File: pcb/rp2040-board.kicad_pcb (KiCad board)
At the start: 4 copper layers, 75 x 48 mm, 51 parts, among them J1 DMX, J2 GPIO, J3 ELRS, J4 OLED, J5 SWD, J6 USB_C_Receptacle_USB2.0_16P, SW1 USB Boot, SW2 RotaryEncoder_Switch, SW3 Reset, U1 W25Q128JVS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

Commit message: board rc3
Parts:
- added C20: 4.7n, Capacitor_SMD:C_0402_1005Metric, F.Cu at (158.4, 86.2)
- added C21: 4.7n, Capacitor_SMD:C_0402_1005Metric, F.Cu at (166.8, 86.2)
- added C22: 22u, Capacitor_SMD:C_0805_2012Metric, F.Cu at (169.0, 82.6)
- added C23: 100n, Capacitor_SMD:C_0402_1005Metric, F.Cu at (161.2, 79.0)
- added C24: 1u, Capacitor_SMD:C_0402_1005Metric, F.Cu at (164.0, 79.0)
- added J7: AUDIO, Connector_PinHeader_2.54mm:PinHeader_1x02_P2.54mm_Vertical, F.Cu at (172.2, 81.3)
- added R14: 1k5, Resistor_SMD:R_0402_1005Metric, F.Cu at (164.0, 86.2)
- added R15: 1k5, Resistor_SMD:R_0402_1005Metric, F.Cu at (161.2, 86.2)
- added R16: 0, Resistor_SMD:R_0603_1608Metric, F.Cu at (154.2, 79.0)
- added U5: OP07CDR, Package_SO:SOIC-8_3.9x4.9mm_P1.27mm, F.Cu at (162.6, 82.6)
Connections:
- U3 pad 41: unconnected-(U3-GPIO29_ADC3-Pad41) -> PWM_AUDIO
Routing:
- net PWM_AUDIO: track 0.00 -> 24.3 mm, vias 0 -> 2
- net Net-(U5-V+): track 0.00 -> 13.4 mm
- net Net-(U5--): track 0.00 -> 13.2 mm
- net Net-(U5-+): track 0.00 -> 9.69 mm
- net ELRS_RX: track 30.7 -> 37.3 mm
- net ELRS_TX: track 33.0 -> 39.4 mm
- net GND: track 80.5 -> 86.8 mm, vias 69 -> 73
- net Net-(C21-Pad1): track 0.00 -> 5.12 mm
- net Net-(J7-Pin_1): track 0.00 -> 3.33 mm
- net +5V: track 95.2 -> 97.3 mm, vias 2 -> 3
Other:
- board text added: "github.com/barycz/rp2040-board Tomas Barak, 2024"

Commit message: board rc4, BOM cleanup
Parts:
- SW1: value USB Boot -> TS-1187A-B-A-B
- SW3: value Reset -> TS-1187A-B-A-B
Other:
- board text added: "GND 3V3 SCK SDA"
- board text added: "GND 5V ERX ETX"
- board text added: "Reset"
- board text added: "USB Boot"

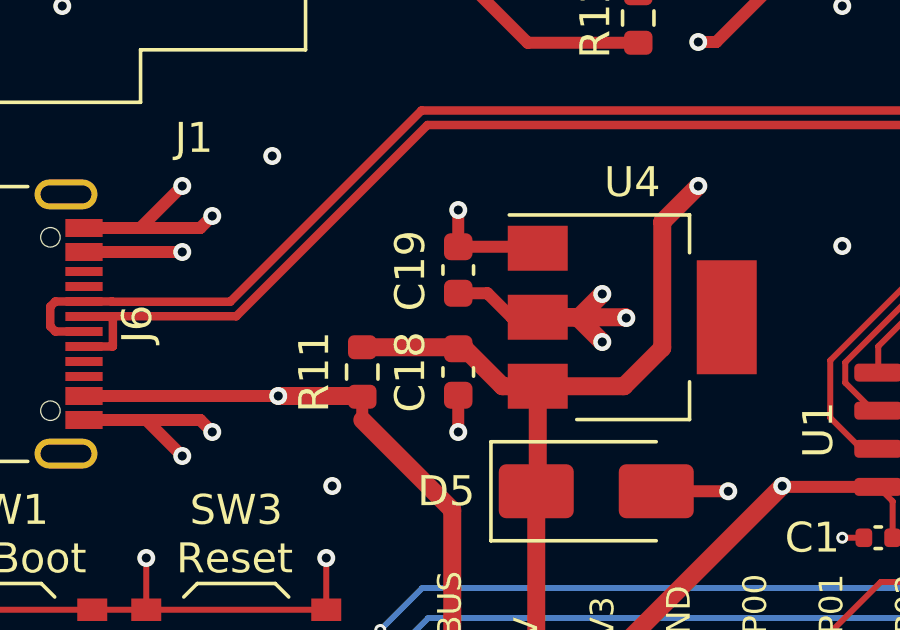
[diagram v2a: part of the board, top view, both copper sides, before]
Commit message: enlarge power supply caps
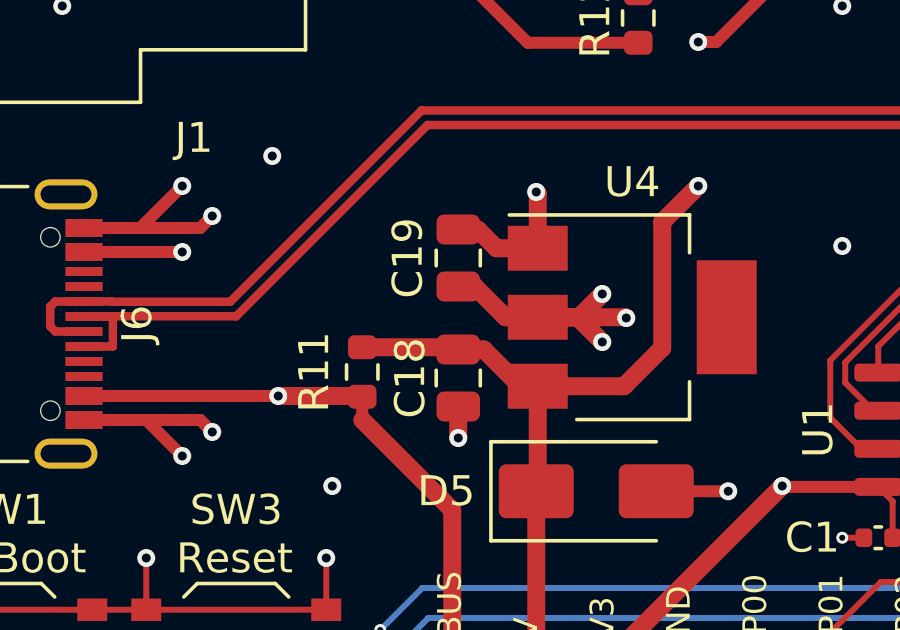
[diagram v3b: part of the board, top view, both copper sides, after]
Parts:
- C18, C19: value 10u -> 22u; footprint Capacitor_SMD:C_0603_1608Metric -> Capacitor_SMD:C_0805_2012Metric
- moved C19 0.40 mm to (119.2, 103.4)
- moved C18 0.20 mm to (119.2, 107.4)
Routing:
- net +3V3: track 169.6 -> 170.6 mm
- net GND: track 86.8 -> 87.6 mm

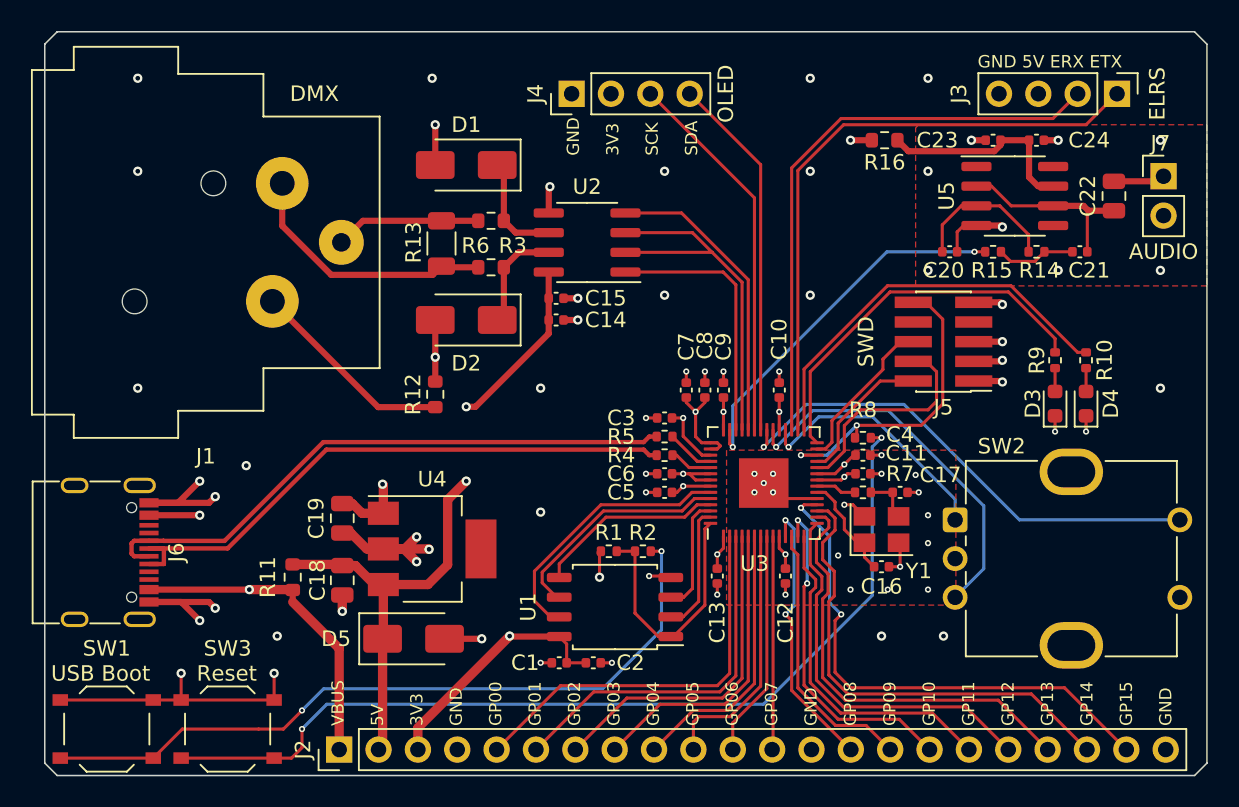
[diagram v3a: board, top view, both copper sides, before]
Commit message: fixed pin assignment issues
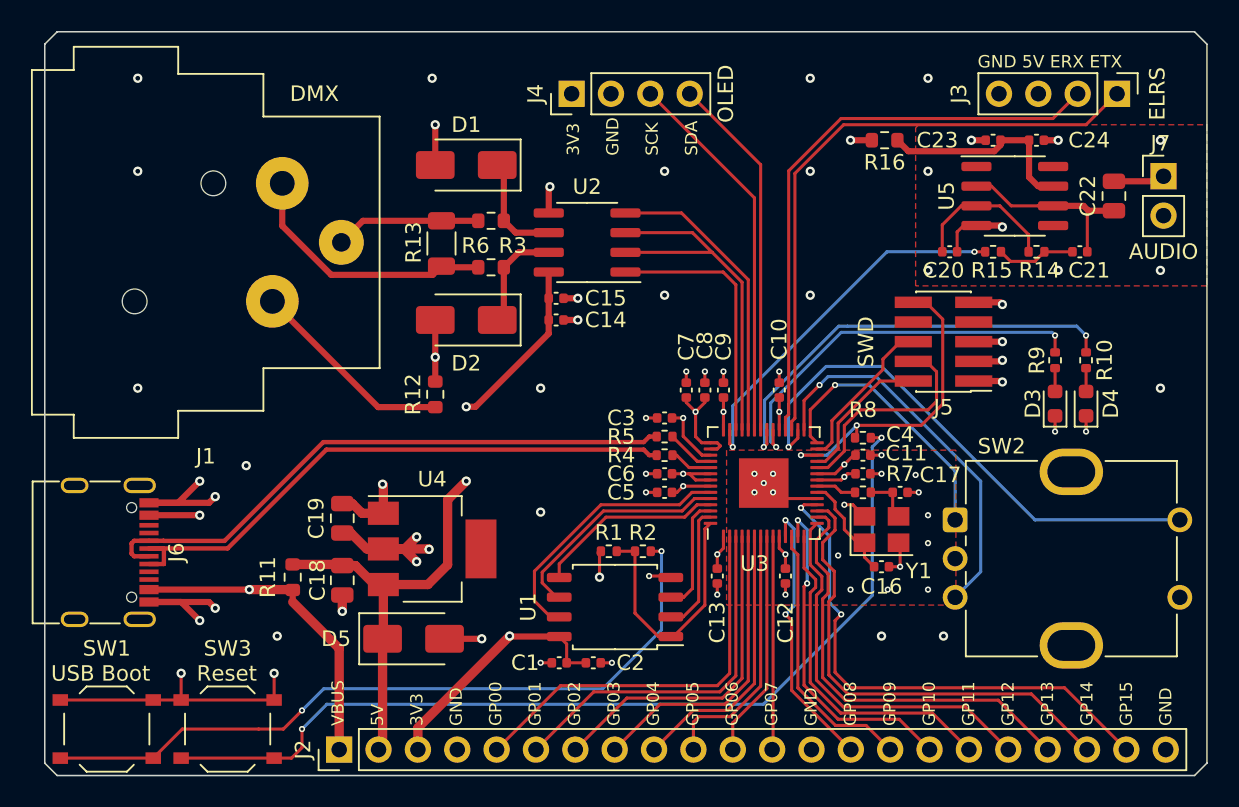
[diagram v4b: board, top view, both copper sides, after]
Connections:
- J4 pad 1: GND -> +3V3
- J4 pad 2: +3V3 -> GND
- U3 pad 28: LED_D1 -> RE_A
- U3 pad 29: LED_D2 -> RE_B
- U3 pad 30: ELRS_TX -> RE_SW
- U3 pad 31: ELRS_RX -> ELRS_TX
- U3 pad 32: RE_A -> ELRS_RX
- U3 pad 34: RE_B -> LED_D1
- U3 pad 35: RE_SW -> LED_D2
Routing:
- net LED_D2: track 26.1 -> 28.4 mm, vias 0 -> 2
- net RE_SW: track 32.3 -> 34.5 mm
- net RE_A: track 16.3 -> 17.8 mm
- net +3V3: track 170.6 -> 169.5 mm
- net LED_D1: track 24.8 -> 25.6 mm, vias 0 -> 2
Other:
- board text added: "3V3 GND SCK SDA"
- board text removed: "GND 3V3 SCK SDA"

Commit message: pin assignment issues fixed
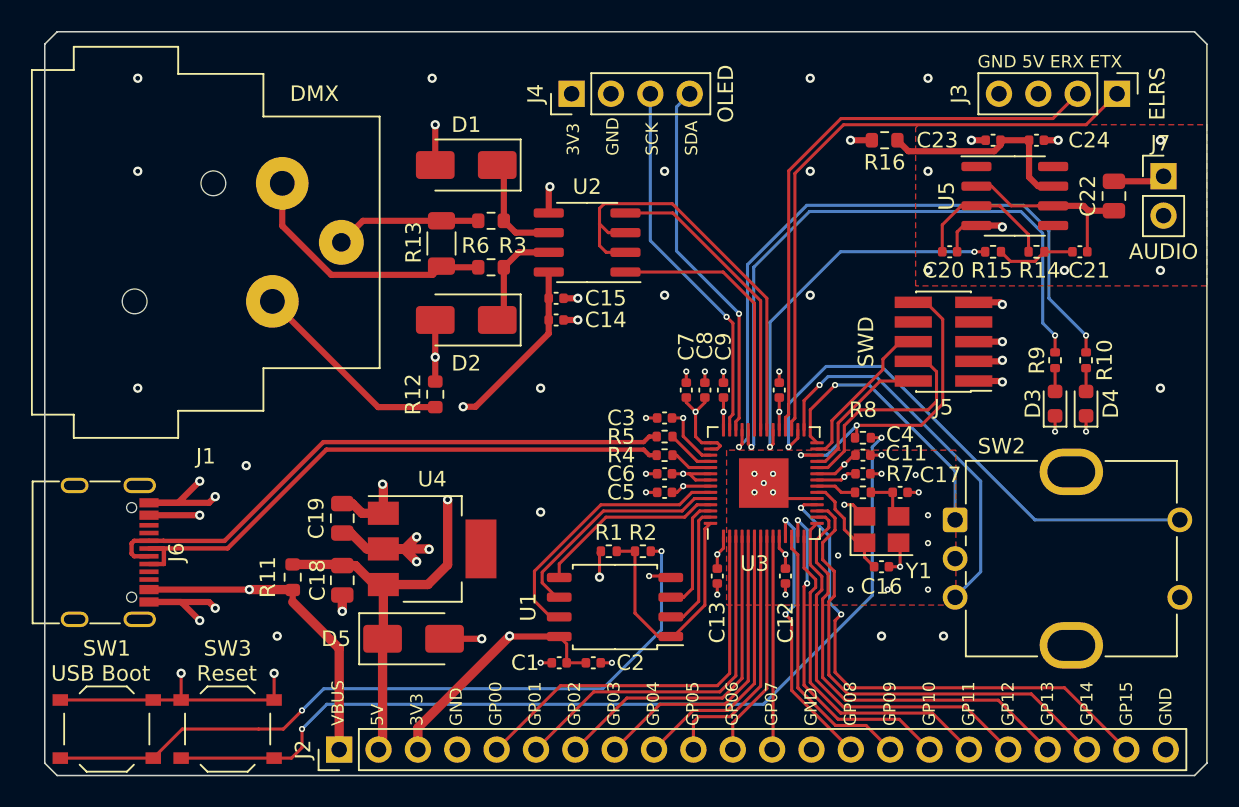
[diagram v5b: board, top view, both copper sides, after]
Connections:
- U2 pad 2: RS485_RE_NDE -> RS485_NRE_DE
- U2 pad 3: RS485_RE_NDE -> RS485_NRE_DE
- U3 pad 34: LED_D1 -> PWM_AUDIO
- U3 pad 35: LED_D2 -> RS485_NRE_DE
- U3 pad 36: OLED_SDA -> RS485_TXD
- U3 pad 37: OLED_SCK -> RS485_RXD
- U3 pad 38: RS485_TXD -> LED_D1
- U3 pad 39: RS485_RE_NDE -> LED_D2
- U3 pad 40: RS485_RXD -> OLED_SDA
- U3 pad 41: PWM_AUDIO -> OLED_SCK
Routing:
- net RS485_NRE_DE: track 0.00 -> 28.1 mm
- net RS485_RE_NDE: track 24.0 -> 0.00 mm
- net LED_D1: track 25.6 -> 41.6 mm
- net LED_D2: track 28.4 -> 43.8 mm
- net PWM_AUDIO: track 24.3 -> 25.0 mm
- net OLED_SCK: track 24.5 -> 24.0 mm, vias 0 -> 1
- net OLED_SDA: track 23.6 -> 23.8 mm, vias 0 -> 1

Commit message: board rc5
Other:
- board text added: "JLCJLCJLCJLC"

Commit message: fabrication tweaks
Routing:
- net +3V3: track 169.5 -> 178.1 mm
- net +1V1: track 26.9 -> 30.3 mm
- net GND: vias 73 -> 75

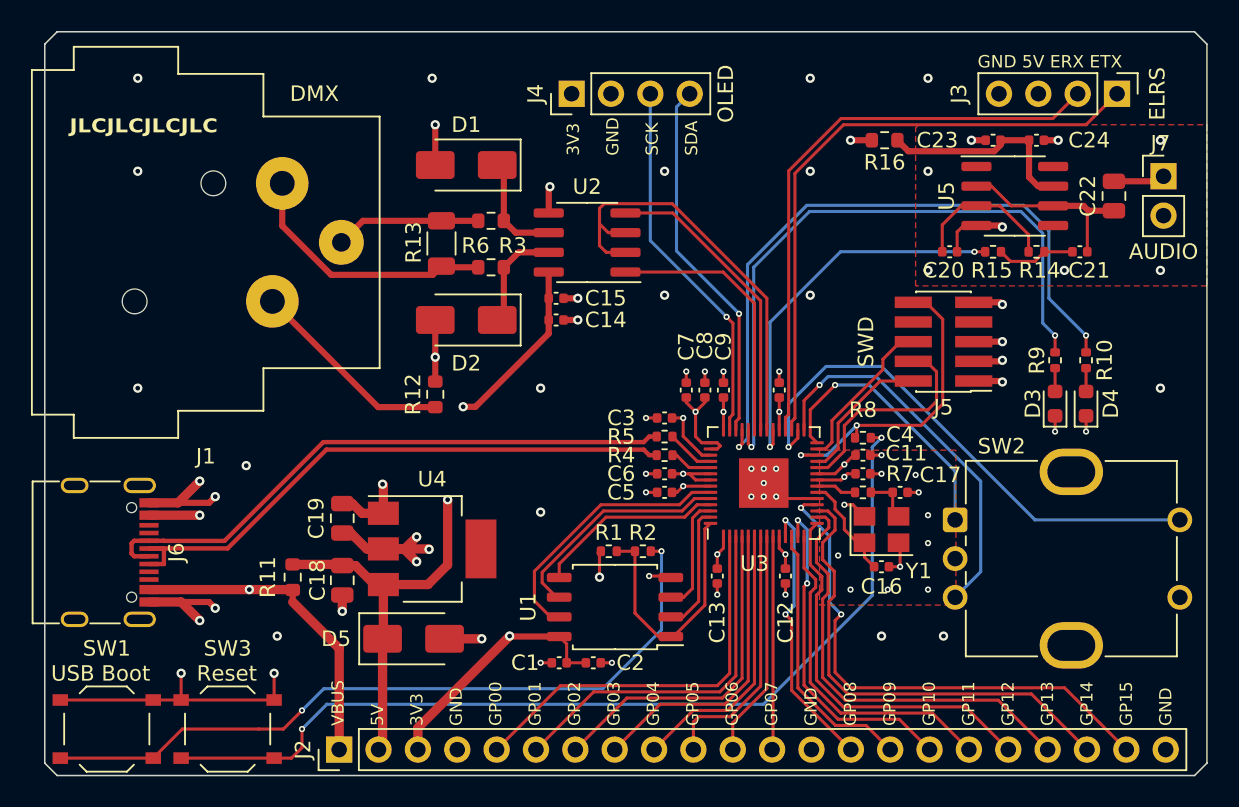
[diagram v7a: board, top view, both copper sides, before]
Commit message: fixed via size
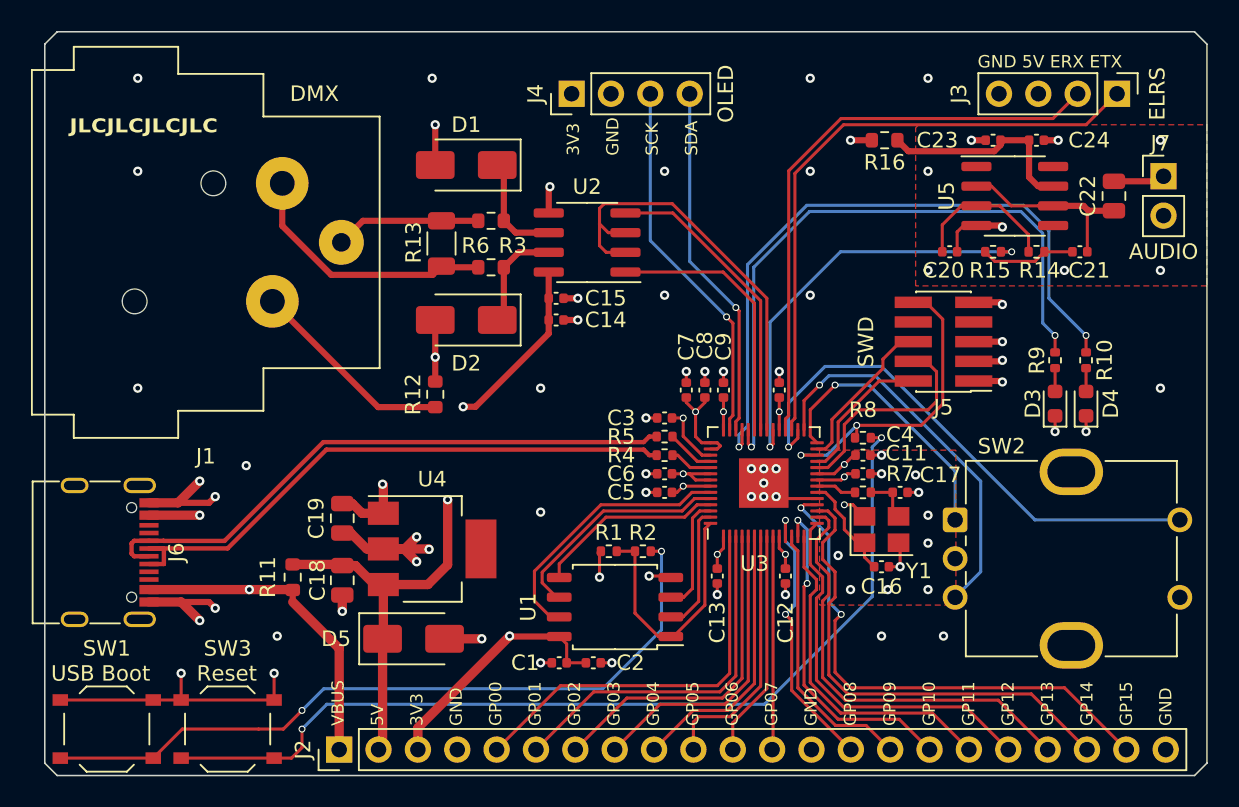
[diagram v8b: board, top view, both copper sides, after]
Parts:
- turned R15 to 180 degrees
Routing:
- net PWM_AUDIO: track 25.0 -> 27.4 mm
- net +3V3: track 178.1 -> 179.8 mm
- net Net-(C21-Pad1): track 5.12 -> 6.14 mm
- net OLED_SDA: track 23.8 -> 23.1 mm
